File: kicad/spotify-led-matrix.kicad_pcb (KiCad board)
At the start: 2 copper layers, 9 parts, among them Q2 SS8050-G, Q3 SS8050-G, U1 ESP32-WROOM-32E, U3 SN74LVC1G14DBV, U4 CP2102N-A01-GQFN28

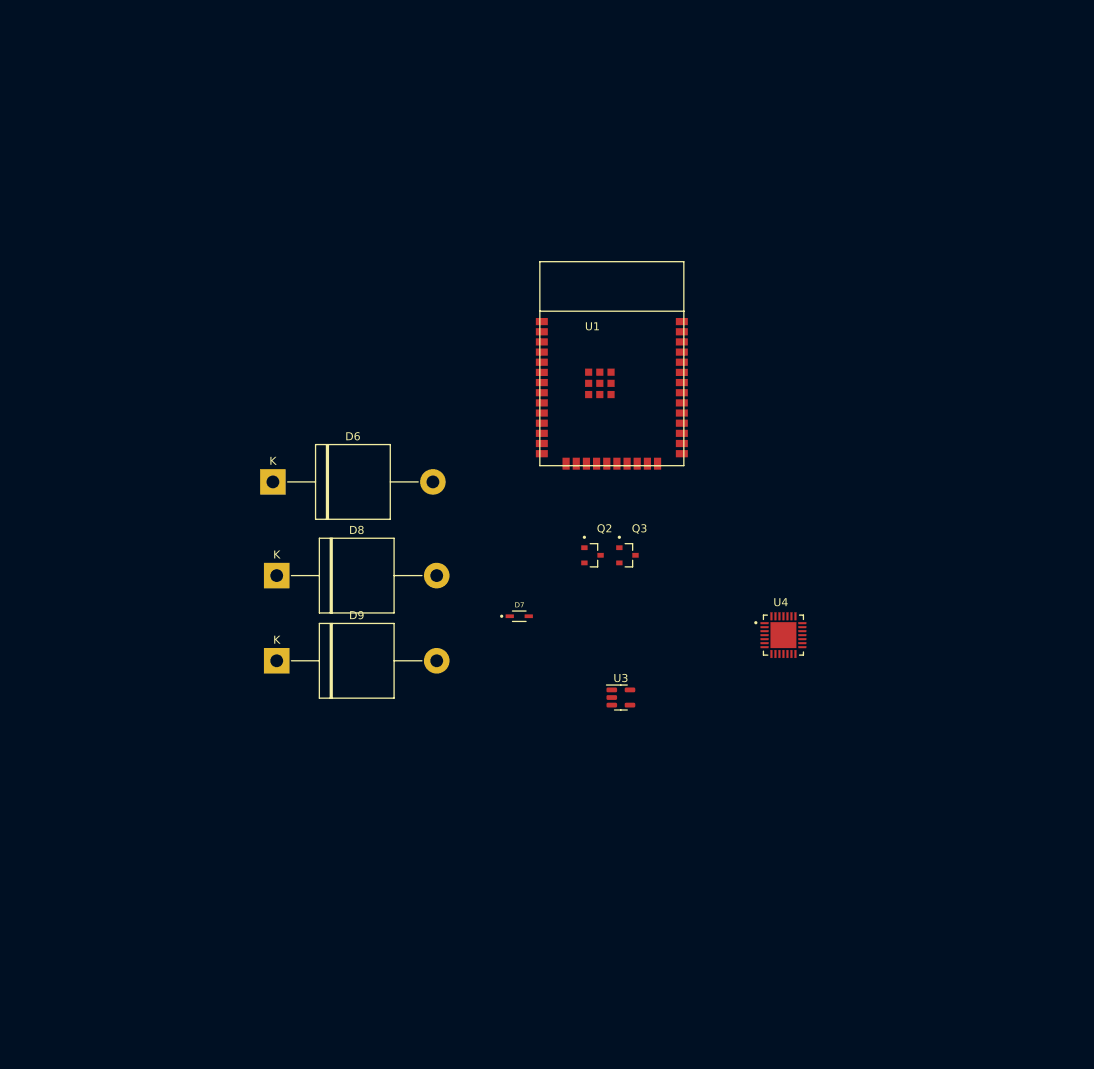
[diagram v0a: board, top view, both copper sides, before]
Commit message: Finished schematic and picked out most parts
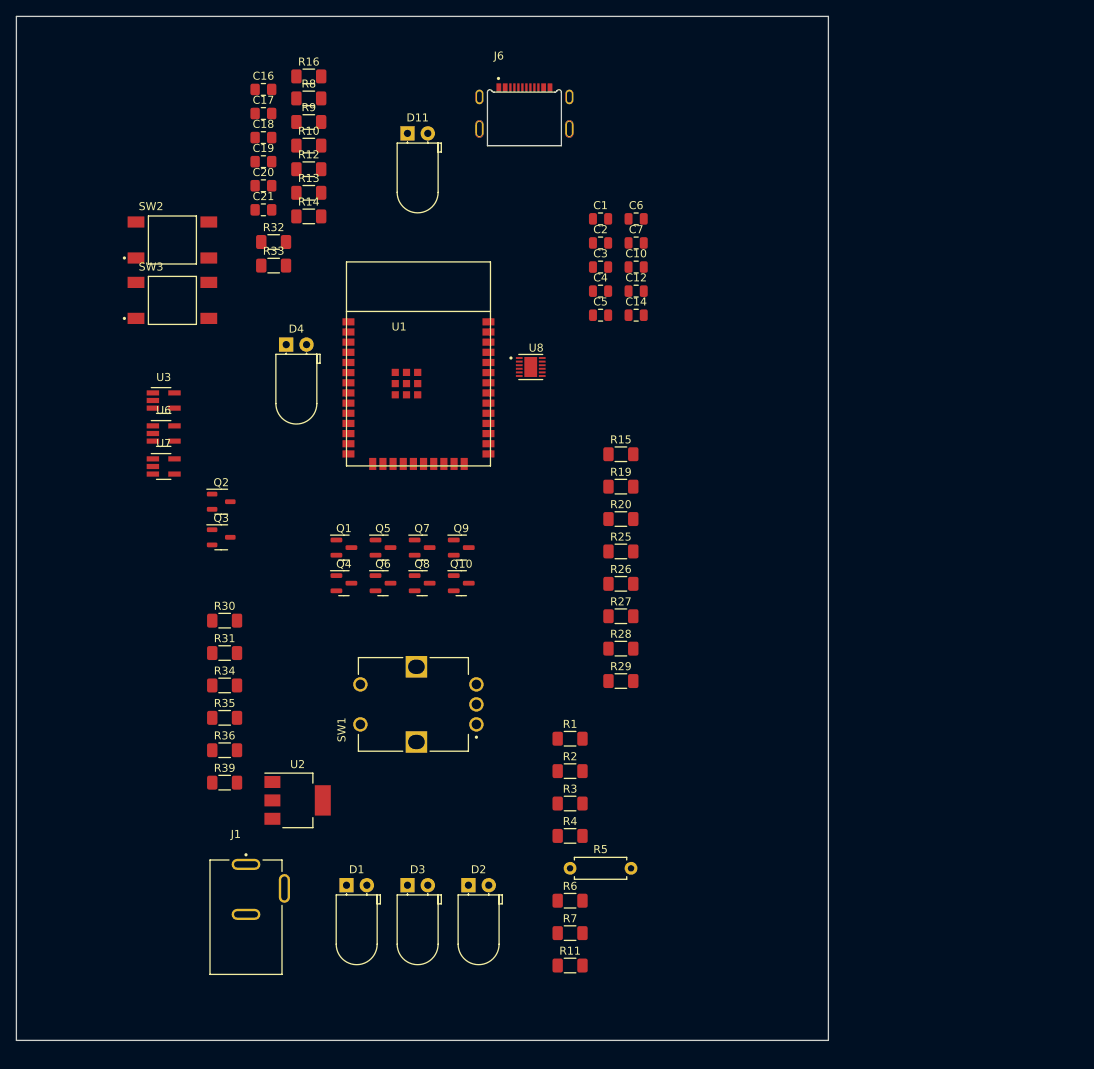
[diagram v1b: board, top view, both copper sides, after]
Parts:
- removed D6, D8, D9: TODO, Diode_THT:D_P600_R-6_P20.00mm_Horizontal
- removed D7: BAT760-7, spotify-led-matrix:SOD2513X120N
- removed U4: CP2102N-A01-GQFN28, spotify-led-matrix:QFN50P500X500X80-29N
- added C1: 1uF, Capacitor_SMD:C_0805_2012Metric, F.Cu at (160.0, 44.3)
- added C10: 0.1uF, Capacitor_SMD:C_0805_2012Metric, F.Cu at (164.5, 50.3)
- added C12: 0.1uF, Capacitor_SMD:C_0805_2012Metric, F.Cu at (164.5, 53.3)
- added C14: 0.1uF, Capacitor_SMD:C_0805_2012Metric, F.Cu at (164.5, 56.4)
- added C16: 100nF, Capacitor_SMD:C_0805_2012Metric_Pad1.18x1.45mm_HandSolder, F.Cu at (117.9, 28.1)
- added C17: 47pF, Capacitor_SMD:C_0805_2012Metric_Pad1.18x1.45mm_HandSolder, F.Cu at (117.9, 31.1)
- added C18: 100nF, Capacitor_SMD:C_0805_2012Metric_Pad1.18x1.45mm_HandSolder, F.Cu at (117.9, 34.1)
- added C19: 47pF, Capacitor_SMD:C_0805_2012Metric_Pad1.18x1.45mm_HandSolder, F.Cu at (117.9, 37.2)
- added C2: 1uF, Capacitor_SMD:C_0805_2012Metric, F.Cu at (160.0, 47.3)
- added C20: 4.7uF, Capacitor_SMD:C_0805_2012Metric_Pad1.18x1.45mm_HandSolder, F.Cu at (117.9, 40.2)
- added C21: 100nF, Capacitor_SMD:C_0805_2012Metric_Pad1.18x1.45mm_HandSolder, F.Cu at (117.9, 43.2)
- added C3: 22uF, Capacitor_SMD:C_0805_2012Metric, F.Cu at (160.0, 50.3)
- added C4: 0.1uF, Capacitor_SMD:C_0805_2012Metric, F.Cu at (160.0, 53.3)
- added C5: 1uF, Capacitor_SMD:C_0805_2012Metric, F.Cu at (160.0, 56.4)
- added C6: 0.1uF, Capacitor_SMD:C_0805_2012Metric, F.Cu at (164.5, 44.3)
- added C7: 0.1uF, Capacitor_SMD:C_0805_2012Metric, F.Cu at (164.5, 47.3)
- added D1: BRIGHTNESS, LED_THT:LED_D5.0mm_Horizontal_O1.27mm_Z9.0mm, F.Cu at (128.3, 127.6)
- added D11: USB, LED_THT:LED_D5.0mm_Horizontal_O1.27mm_Z9.0mm, F.Cu at (135.9, 33.6)
- added D2: MODES, LED_THT:LED_D5.0mm_Horizontal_O1.27mm_Z9.0mm, F.Cu at (143.5, 127.6)
- added D3: VOLUME, LED_THT:LED_D5.0mm_Horizontal_O1.27mm_Z9.0mm, F.Cu at (135.9, 127.6)
- added D4: DEV, LED_THT:LED_D5.0mm_Horizontal_O1.27mm_Z9.0mm, F.Cu at (120.7, 60.0)
- added J1: +5V, spotify-led-matrix:54-00166, F.Cu at (115.7, 131.2)
- added J6: USB_C_Receptacle_USB2.0, spotify-led-matrix:MOLEX_2169900003, F.Cu at (150.5, 33.1)
- added Q1: IRLML6244TRPBF, Package_TO_SOT_SMD:SOT-23, F.Cu at (127.9, 85.4)
- added Q10: IRLML6244TRPBF, Package_TO_SOT_SMD:SOT-23, F.Cu at (142.6, 89.8)
- added Q4: IRLML6244TRPBF, Package_TO_SOT_SMD:SOT-23, F.Cu at (127.9, 89.8)
- added Q5: IRLML6244TRPBF, Package_TO_SOT_SMD:SOT-23, F.Cu at (132.8, 85.4)
- added Q6: IRLML6244TRPBF, Package_TO_SOT_SMD:SOT-23, F.Cu at (132.8, 89.8)
- added Q7: IRLML6244TRPBF, Package_TO_SOT_SMD:SOT-23, F.Cu at (137.7, 85.4)
- added Q8: IRLML6244TRPBF, Package_TO_SOT_SMD:SOT-23, F.Cu at (137.7, 89.8)
- added Q9: IRLML6244TRPBF, Package_TO_SOT_SMD:SOT-23, F.Cu at (142.6, 85.4)
- added R1: 82, Resistor_SMD:R_1206_3216Metric_Pad1.30x1.75mm_HandSolder, F.Cu at (156.2, 109.3)
- added R10: 22, Resistor_SMD:R_1206_3216Metric_Pad1.30x1.75mm_HandSolder, F.Cu at (123.5, 35.1)
- added R11: 1k, Resistor_SMD:R_1206_3216Metric_Pad1.30x1.75mm_HandSolder, F.Cu at (156.2, 137.6)
- added R12: 22, Resistor_SMD:R_1206_3216Metric_Pad1.30x1.75mm_HandSolder, F.Cu at (123.5, 38.1)
- added R13: 0, Resistor_SMD:R_1206_3216Metric_Pad1.30x1.75mm_HandSolder, F.Cu at (123.5, 41.0)
- added R14: 22, Resistor_SMD:R_1206_3216Metric_Pad1.30x1.75mm_HandSolder, F.Cu at (123.5, 44.0)
- added R15: 120, Resistor_SMD:R_1206_3216Metric_Pad1.30x1.75mm_HandSolder, F.Cu at (162.6, 73.7)
- added R16: 0, Resistor_SMD:R_1206_3216Metric_Pad1.30x1.75mm_HandSolder, F.Cu at (123.5, 26.5)
- added R19: 10k, Resistor_SMD:R_1206_3216Metric_Pad1.30x1.75mm_HandSolder, F.Cu at (162.6, 77.8)
- added R2: 82, Resistor_SMD:R_1206_3216Metric_Pad1.30x1.75mm_HandSolder, F.Cu at (156.2, 113.3)
- added R20: 10k, Resistor_SMD:R_1206_3216Metric_Pad1.30x1.75mm_HandSolder, F.Cu at (162.6, 81.8)
- added R25: 10k, Resistor_SMD:R_1206_3216Metric_Pad1.30x1.75mm_HandSolder, F.Cu at (162.6, 85.9)
- added R26: 1k, Resistor_SMD:R_1206_3216Metric_Pad1.30x1.75mm_HandSolder, F.Cu at (162.6, 89.9)
- added R27: 10k, Resistor_SMD:R_1206_3216Metric_Pad1.30x1.75mm_HandSolder, F.Cu at (162.6, 94.0)
- added R28: 1k, Resistor_SMD:R_1206_3216Metric_Pad1.30x1.75mm_HandSolder, F.Cu at (162.6, 98.0)
- added R29: 10k, Resistor_SMD:R_1206_3216Metric_Pad1.30x1.75mm_HandSolder, F.Cu at (162.6, 102.1)
- added R3: 82, Resistor_SMD:R_1206_3216Metric_Pad1.30x1.75mm_HandSolder, F.Cu at (156.2, 117.4)
- added R30: 10k, Resistor_SMD:R_1206_3216Metric_Pad1.30x1.75mm_HandSolder, F.Cu at (113.0, 94.5)
- added R31: 10k, Resistor_SMD:R_1206_3216Metric_Pad1.30x1.75mm_HandSolder, F.Cu at (113.0, 98.6)
- added R32: 27, Resistor_SMD:R_1206_3216Metric_Pad1.30x1.75mm_HandSolder, F.Cu at (119.2, 47.2)
- added R33: 27, Resistor_SMD:R_1206_3216Metric_Pad1.30x1.75mm_HandSolder, F.Cu at (119.2, 50.1)
- added R34: 10k, Resistor_SMD:R_1206_3216Metric_Pad1.30x1.75mm_HandSolder, F.Cu at (113.0, 102.6)
- added R35: 10k, Resistor_SMD:R_1206_3216Metric_Pad1.30x1.75mm_HandSolder, F.Cu at (113.0, 106.7)
- added R36: 10k, Resistor_SMD:R_1206_3216Metric_Pad1.30x1.75mm_HandSolder, F.Cu at (113.0, 110.7)
- added R39: 120, Resistor_SMD:R_1206_3216Metric_Pad1.30x1.75mm_HandSolder, F.Cu at (113.0, 114.8)
- added R4: 10k, Resistor_SMD:R_1206_3216Metric_Pad1.30x1.75mm_HandSolder, F.Cu at (156.2, 121.4)
- added R5: 0, Resistor_THT:R_Axial_DIN0207_L6.3mm_D2.5mm_P7.62mm_Horizontal, F.Cu at (156.2, 125.5)
- added R6: 10k, Resistor_SMD:R_1206_3216Metric_Pad1.30x1.75mm_HandSolder, F.Cu at (156.2, 129.5)
- added R7: 10k, Resistor_SMD:R_1206_3216Metric_Pad1.30x1.75mm_HandSolder, F.Cu at (156.2, 133.6)
- added R8: 22, Resistor_SMD:R_1206_3216Metric_Pad1.30x1.75mm_HandSolder, F.Cu at (123.5, 29.2)
- added R9: 0, Resistor_SMD:R_1206_3216Metric_Pad1.30x1.75mm_HandSolder, F.Cu at (123.5, 32.2)
- added SW1: SELECT, spotify-led-matrix:CUI_ACZ11BR1E-20FD1-20C, F.Cu at (137.0, 105.0)
- added SW2: EN, spotify-led-matrix:SW_TL3301DF160QG, F.Cu at (106.5, 47.0)
- added SW3: BOOT, spotify-led-matrix:SW_TL3301DF160QG, F.Cu at (106.5, 54.5)
- added U2: 5V_TO_3V3, Package_TO_SOT_SMD:SOT-223-3_TabPin2, F.Cu at (122.2, 117.0)
- added U6: MC74HC1G14DTT1G, Package_TO_SOT_SMD:SOT-23-5_HandSoldering, F.Cu at (105.4, 71.1)
- added U7: MC74HC1G14DTT1G, Package_TO_SOT_SMD:SOT-23-5_HandSoldering, F.Cu at (105.4, 75.3)
- added U8: FT234XD-R, spotify-led-matrix:SON45P300X300X80-13N, F.Cu at (151.3, 62.8)
- Q2, Q3: footprint spotify-led-matrix:TRANS_SS8050-G -> Package_TO_SOT_SMD:SOT-23-3
- U3: value SN74LVC1G14DBV -> MC74HC1G14DTT1G; footprint Package_TO_SOT_SMD:SOT-23-5 -> Package_TO_SOT_SMD:SOT-23-5_HandSoldering
- moved U3 68.2 mm to (105.4, 67.0)
- moved Q3 50.8 mm to (112.6, 84.1)
- moved Q2 46.9 mm to (112.6, 79.7)
- moved U1 24.2 mm to (137.3, 65.4)
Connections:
- net /A renamed /CS_A
- net /B renamed /CS_B
- net /C renamed /CS_C
- net /D renamed /CS_D
- net /E renamed /CS_E
- net /GPIO16 renamed /~{OE}
- net /GPIO22 renamed /~{LAT}
- net /PI_R1 renamed /R1_IN
- Q2 pad 3: /EN -> /EN_AUTO
- Q3 pad 2: /BOOT -> /BOOT_AUTO
- Q3 pad 3: /DTR -> /CTS
- U1 pad 24: Net-(D1-A) -> /DEV
- U3 pad 4: /SELECT -> Net-(Q4-S)
- U3 pad 5: +3V3 -> +5V
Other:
- board outline added: 101.5 x 128 mm

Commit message: Working out gitignore issues.
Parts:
- removed J6: USB_C_Receptacle_USB2.0, spotify-led-matrix:MOLEX_2169900003
- removed Q1: IRLML6244TRPBF, Package_TO_SOT_SMD:SOT-23
- removed R13, R9: 0, Resistor_SMD:R_1206_3216Metric_Pad1.30x1.75mm_HandSolder
- removed R5: 0, Resistor_THT:R_Axial_DIN0207_L6.3mm_D2.5mm_P7.62mm_Horizontal
- removed R6: 10k, Resistor_SMD:R_1206_3216Metric_Pad1.30x1.75mm_HandSolder
- added F1: Fuse, Fuse:Fuse_1206_3216Metric_Pad1.42x1.75mm_HandSolder, F.Cu at (120.0, 74.8)
- added J2: DSIPLAY_IN, Connector_PinSocket_2.54mm:PinSocket_2x10_P2.54mm_Vertical, F.Cu at (201.3, 76.1)
- added J4: DISPLAY_OUT, Connector_PinHeader_2.54mm:PinHeader_2x08_P2.54mm_Horizontal, F.Cu at (207.0, 78.8)
- added J5: USB_C_Receptacle_USB2.0, spotify-led-matrix:MOLEX_2169900003, F.Cu at (174.8, 41.1)
- SW1: value SELECT -> MODE_SELECT
- moved R11 66.8 mm to (125.9, 78.1)
- moved C16 66.7 mm to (178.0, 57.0)
- moved C17 66.7 mm to (178.0, 60.0)
- moved C18 66.7 mm to (178.0, 63.0)
- moved C19 66.7 mm to (178.0, 66.0)
- moved C20 66.7 mm to (178.0, 69.0)
- moved C21 66.7 mm to (178.0, 72.0)
- moved R8 65.4 mm to (120.0, 94.6)
- moved R16 64.8 mm to (125.9, 91.3)
- moved R7 55.7 mm to (120.0, 91.3)
- moved U2 53.6 mm to (146.0, 69.0)
- moved R4 49.3 mm to (120.0, 88.0)
- moved R3 48.8 mm to (120.0, 84.7)
- moved R2 48.3 mm to (120.0, 81.4)
- moved U7 48.1 mm to (136.2, 112.2)
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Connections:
- C10 pad 1: Net-(C10-Pad1) -> /BOOT_SW
- C6 pad 1: Net-(C6-Pad1) -> /EN_SW
- Q4 pad 3: /SELECT -> /MODE_SELECT
- R12 pad 2: /EN_BTN -> /EN_SW
- R30 pad 1: /SELECT -> /MODE_SELECT
- R8 pad 2: /BOOT_BTN -> /BOOT_SW
- SW1 pad P1: (no net) -> unconnected-(SW1-PadP1)
- SW1 pad P2: (no net) -> unconnected-(SW1-PadP2)
- SW2 pad 2: Net-(C6-Pad1) -> /EN_SW
- SW3 pad 2: Net-(C10-Pad1) -> /BOOT_SW
- U1 pad 10: unconnected-(U1-IO25-Pad10) -> /ROTARY_B
- U1 pad 11: unconnected-(U1-IO26-Pad11) -> /ROTARY_A
- U1 pad 13: /TMS -> /CLK
- U1 pad 14: /CLK -> unconnected-(U1-IO12-Pad14)
- U1 pad 26: unconnected-(U1-IO4-Pad26) -> /VOLUME
- U1 pad 28: unconnected-(U1-IO17-Pad28) -> /BRIGHTNESS
- U1 pad 33: unconnected-(U1-IO21-Pad33) -> /MODES
- U1 pad 9: unconnected-(U1-IO33-Pad9) -> /MODE_SELECT
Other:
- board size 101.5 x 128 mm -> 100.5 x 118 mm
